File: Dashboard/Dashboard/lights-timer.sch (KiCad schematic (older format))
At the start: 5 parts, among them U1 TS555

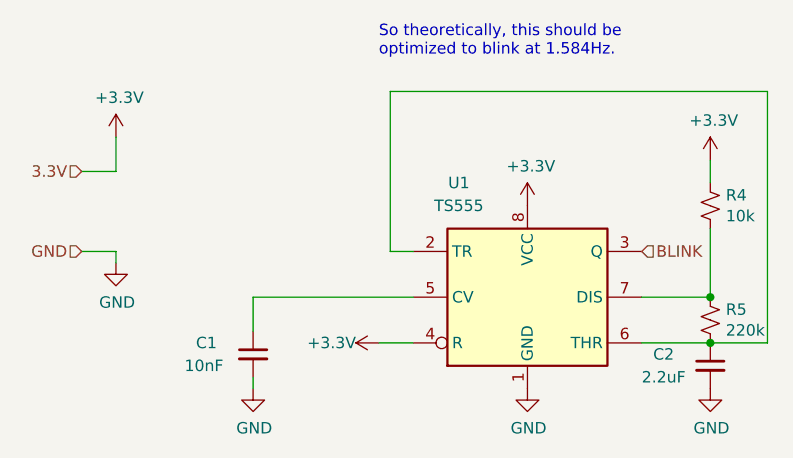
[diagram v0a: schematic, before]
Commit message: Add redundant potentiometers and relabel components.
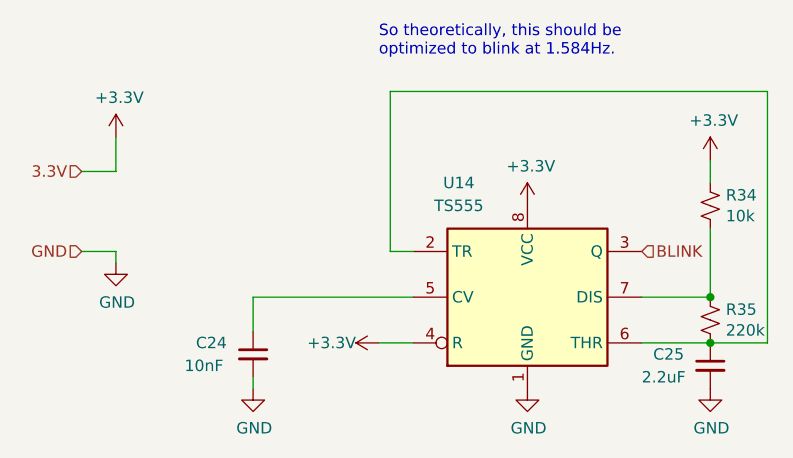
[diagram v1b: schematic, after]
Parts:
- C24: renamed from C1; footprint (none) -> Capacitor_SMD:C_0805_2012Metric
- C25: renamed from C2; footprint (none) -> Capacitor_SMD:C_0805_2012Metric
- R34: renamed from R4; footprint (none) -> Resistor_SMD:R_0805_2012Metric
- R35: renamed from R5; footprint (none) -> Resistor_SMD:R_0805_2012Metric
- renumbered U1 to U14
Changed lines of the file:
@@
 $Descr A4 11693 8268
 encoding utf-8
-Sheet 6 6
+Sheet 3 6
 Title ""
 Date ""
@@
 $EndDescr
 $Comp
-L Dash2-rescue:NE555-Timer U1
+L Dash2-rescue:NE555-Timer U14
 U 1 1 5EBF0D26
 P 5650 3600
-F 0 "U1" H 5350 4100 50  0000 C CNN
+F 0 "U14" H 5350 4100 50  0000 C CNN
 F 1 "TS555" H 5350 4000 50  0000 C CNN
 F 2 "" H 5650 3600 50  0001 C CNN
@@
 $EndComp
 $Comp
-L power:+3.3V #PWR0178
+L power:+3.3V #PWR091
 U 1 1 5EBF2615
 P 5650 3200
-F 0 "#PWR0178" H 5650 3050 50  0001 C CNN
+F 0 "#PWR091" H 5650 3050 50  0001 C CNN
 F 1 "+3.3V" H 5665 3373 50  0000 C CNN
 F 2 "" H 5650 3200 50  0001 C CNN
@@
 $EndComp
 $Comp
-L power:GND #PWR0179
+L power:GND #PWR092
 U 1 1 5EBF28CB
 P 5650 4000
-F 0 "#PWR0179" H 5650 3750 50  0001 C CNN
+F 0 "#PWR092" H 5650 3750 50  0001 C CNN
 F 1 "GND" H 5655 3827 50  0000 C CNN
 F 2 "" H 5650 4000 50  0001 C CNN
@@
 $EndComp
 $Comp
-L power:+3.3V #PWR0180
+L power:+3.3V #PWR090
 U 1 1 5EBF2A33
 P 5000 3800
-F 0 "#PWR0180" H 5000 3650 50  0001 C CNN
+F 0 "#PWR090" H 5000 3650 50  0001 C CNN
 F 1 "+3.3V" V 5000 3900 50  0000 L CNN
 F 2 "" H 5000 3800 50  0001 C CNN
@@
 	4450 3600 4450 3750
 $Comp
-L Device:C_Small C1
+L Device:C_Small C24
 U 1 1 5EBF316A
 P 4450 3850
-F 0 "C1" H 4200 3900 50  0000 L CNN
+F 0 "C24" H 4200 3900 50  0000 L CNN
 F 1 "10nF" H 4150 3800 50  0000 L CNN
-F 2 "" H 4450 3850 50  0001 C CNN
+F 2 "Capacitor_SMD:C_0805_2012Metric" H 4450 3850 50  0001 C CNN
 F 3 "~" H 4450 3850 50  0001 C CNN
 	1    4450 3850
@@
 $EndComp
 $Comp
-L power:GND #PWR0181
+L power:GND #PWR089
 U 1 1 5EBF3A8A
 P 4450 4000
-F 0 "#PWR0181" H 4450 3750 50  0001 C CNN
+F 0 "#PWR089" H 4450 3750 50  0001 C CNN
 F 1 "GND" H 4455 3827 50  0000 C CNN
 F 2 "" H 4450 4000 50  0001 C CNN
@@
 	6150 3800 6450 3800
 $Comp
-L power:GND #PWR0182
+L power:GND #PWR094
 U 1 1 5EBF43E5
 P 6450 4000
-F 0 "#PWR0182" H 6450 3750 50  0001 C CNN
+F 0 "#PWR094" H 6450 3750 50  0001 C CNN
 F 1 "GND" H 6455 3827 50  0000 C CNN
 F 2 "" H 6450 4000 50  0001 C CNN
@@
 	6450 3600 6150 3600
 $Comp
-L power:+3.3V #PWR0183
+L power:+3.3V #PWR093
 U 1 1 5EBF71CD
 P 6450 3000
-F 0 "#PWR0183" H 6450 2850 50  0001 C CNN
+F 0 "#PWR093" H 6450 2850 50  0001 C CNN
 F 1 "+3.3V" H 6465 3173 50  0000 C CNN
 F 2 "" H 6450 3000 50  0001 C CNN
@@
 GND
 $Comp
-L power:+3.3V #PWR0184
+L power:+3.3V #PWR087
 U 1 1 5EBFBD16
 P 3850 2900
-F 0 "#PWR0184" H 3850 2750 50  0001 C CNN
+F 0 "#PWR087" H 3850 2750 50  0001 C CNN
 F 1 "+3.3V" H 3865 3073 50  0000 C CNN
 F 2 "" H 3850 2900 50  0001 C CNN
@@
 	3850 3050 3700 3050
 $Comp
-L power:GND #PWR0185
+L power:GND #PWR088
 U 1 1 5EBFC31C
 P 3850 3450
-F 0 "#PWR0185" H 3850 3200 50  0001 C CNN
+F 0 "#PWR088" H 3850 3200 50  0001 C CNN
 F 1 "GND" H 3855 3277 50  0000 C CNN
 F 2 "" H 3850 3450 50  0001 C CNN
@@
 	3850 3400 3700 3400
 $Comp
-L Device:C_Small C2
+L Device:C_Small C25
 U 1 1 5EBF3E10
 P 6450 3900
-F 0 "C2" H 6200 3950 50  0000 L CNN
+F 0 "C25" H 6200 3950 50  0000 L CNN
 F 1 "2.2uF" H 6150 3850 50  0000 L CNN
-F 2 "" H 6450 3900 50  0001 C CNN
+F 2 "Capacitor_SMD:C_0805_2012Metric" H 6450 3900 50  0001 C CNN
 F 3 "~" H 6450 3900 50  0001 C CNN
 	1    6450 3900
@@
 $EndComp
 $Comp
-L Device:R_Small_US R5
+L Device:R_Small_US R35
 U 1 1 5EBF5CCC
 P 6450 3700
-F 0 "R5" H 6518 3746 50  0000 L CNN
+F 0 "R35" H 6518 3746 50  0000 L CNN
 F 1 "220k" H 6518 3655 50  0000 L CNN
-F 2 "" H 6450 3700 50  0001 C CNN
+F 2 "Resistor_SMD:R_0805_2012Metric" H 6450 3700 50  0001 C CNN
 F 3 "~" H 6450 3700 50  0001 C CNN
 	1    6450 3700
@@
 	6450 3100 6450 3000
 $Comp
-L Device:R_Small_US R4
+L Device:R_Small_US R34
 U 1 1 5EBF6EC8
 P 6450 3200
-F 0 "R4" H 6518 3246 50  0000 L CNN
+F 0 "R34" H 6518 3246 50  0000 L CNN
 F 1 "10k" H 6518 3155 50  0000 L CNN
-F 2 "" H 6450 3200 50  0001 C CNN
+F 2 "Resistor_SMD:R_0805_2012Metric" H 6450 3200 50  0001 C CNN
 F 3 "~" H 6450 3200 50  0001 C CNN
 	1    6450 3200
